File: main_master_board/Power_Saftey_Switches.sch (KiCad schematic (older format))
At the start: 2 parts

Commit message: Added lots of things. current/voltage monitoring. and other stuff
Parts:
- added C?: 48nF, symbol C_Small
- added C?: 2uF, symbol C_Small
- added C? (x2): 100nF, symbol C_Small
- added C?: 100uF, symbol C_Small
- added C?: 100nF, symbol C
- added D? (x2): DA2S10100L, symbol D_Small
- added P?: CONN_01X05, symbol CONN_01X05
- added Q?: LT1910, SO_8, symbol LT1910
- added R?: 0.0025, symbol R
- added R? (x3): 5K, symbol R
- added R? (x2): 1K, symbol R
- added R? (x3): 10K, symbol R
- added SW?: SWITCH_SPST, symbol SWITCH_SPST
- added U?: 74HC1G126, symbol 74AHC1G126
- added U?: PIC12(L)F1571/2, symbol PIC12(L)F1571/2
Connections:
- net labels added: 3V3, GND, KS_nFault, KS_physical_in, KS_physical_out, KS_uC, KS_watchdog, MCLR_KS, Motor_en, PGEC_KS, PGED_KS, Sense, Vmain, Vmotors, main_gate, uC_KS_1, uC_KS_2
- wire segments 7 -> 106
- no-connect marks 0 -> 1
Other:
- note added: "Do not get\n74HCT1G126\nvariant"
- note added: "KS_uC"
- note added: "KS_uC_programmer"
- note added: "Manual switch to \nturn motors off"
- note added: "TVS to \nkeep <20V"
- moved on the sheet: D?, Q?

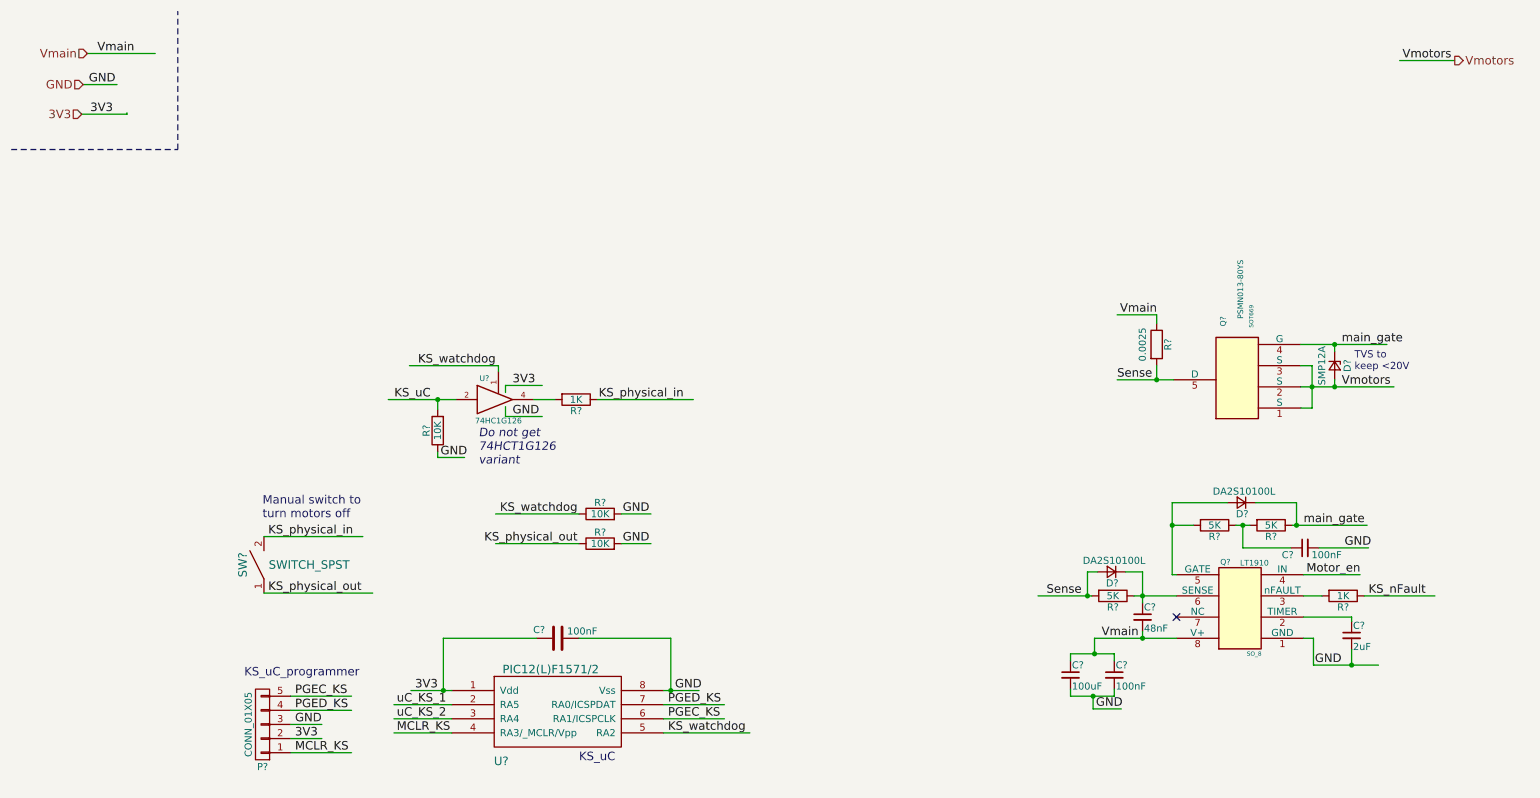
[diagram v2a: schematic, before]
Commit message: Updated some of the schematics and started assigning footprints
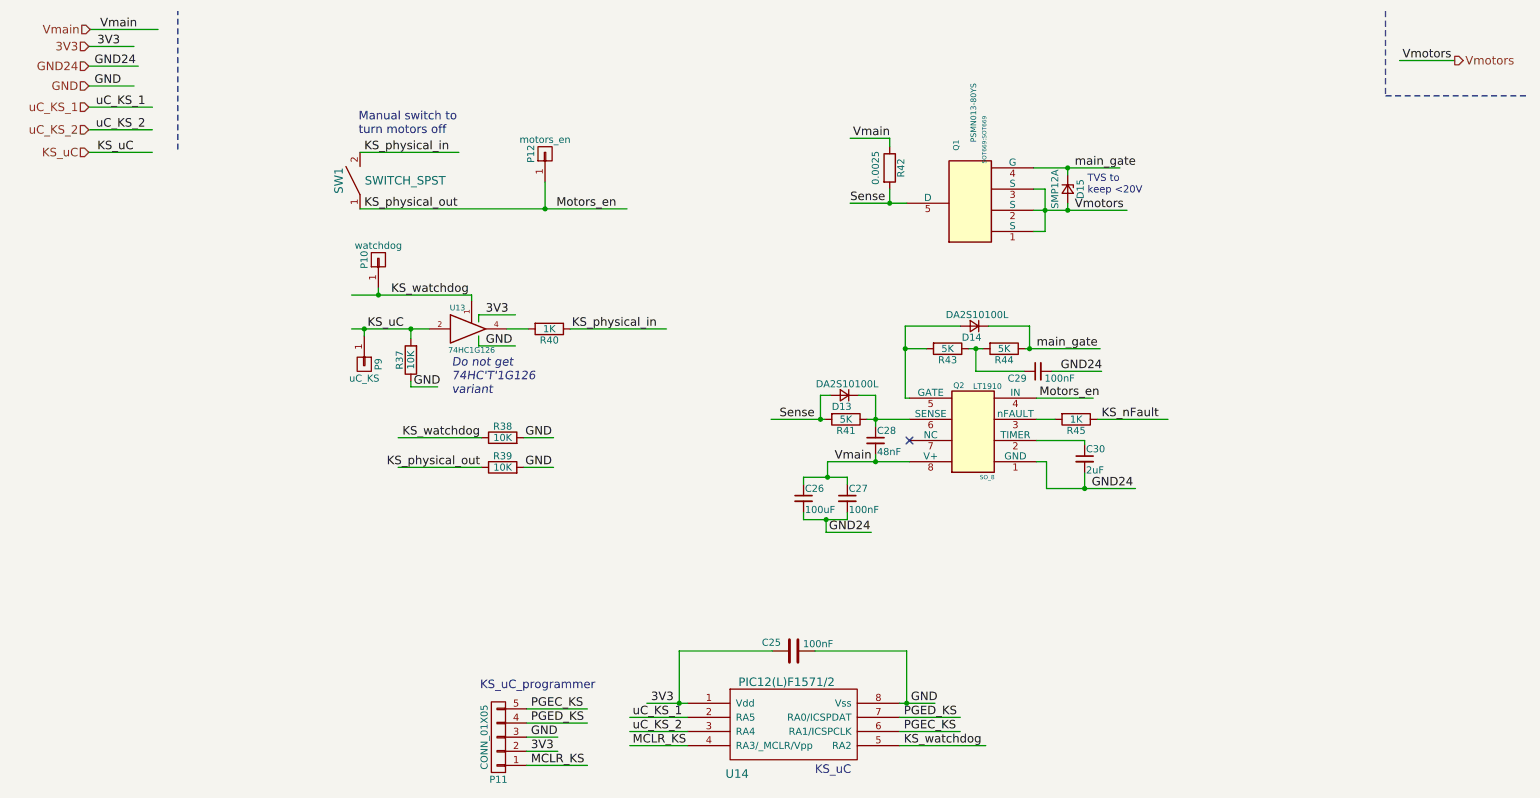
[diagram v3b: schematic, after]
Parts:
- added P10: watchdog, symbol CONN_01X01
- added P12: motors_en, symbol CONN_01X01
- added P9: uC_KS, symbol CONN_01X01
- Q1: renamed from Q?; footprint SOT669 -> SOT669:SOT669
- gave numbers to parts that had none: 23
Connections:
- net labels added: GND24, Motors_en
- net labels removed: Motor_en
- wire segments 106 -> 94
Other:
- note added: "Do not get\n74HC'T'1G126\nvariant"
- note removed: "Do not get\n74HCT1G126\nvariant"
- moved on the sheet: C25, C26, C27, C28, C29, C30, D13, D14, D15, P11, Q1, Q2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

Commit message: Updating the footprints and components list. still working on it
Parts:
- R37, R38, R39, R40, R41, R42, R43, R44, R45: footprint (none) -> Resistors_SMD:R_0603
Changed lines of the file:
@@
 LIBS:FDS4935A
 LIBS:Si1900DL
-LIBS:Amplifiers
-LIBS:Connectors
-LIBS:DataStorage
-LIBS:Diodes
-LIBS:Microprocessors
-LIBS:MiscellaneousDevices
-LIBS:Passives
-LIBS:PMOD
-LIBS:PowerComponents
-LIBS:RepeaterParts
-LIBS:RF_OEM_Parts
 LIBS:Sensors
-LIBS:TransistorParts
 LIBS:LP3852-3.3
 LIBS:0s102011ma1qn1
@@
 F 0 "R42" V 6780 1590 50  0000 C CNN
 F 1 "0.0025" V 6600 1590 50  0000 C CNN
-F 2 "" V 6630 1590 50  0001 C CNN
+F 2 "Resistors_SMD:R_0603" V 6630 1590 50  0001 C CNN
 F 3 "" H 6700 1590 50  0000 C CNN
 	1    6700 1590
@@
 F 0 "R41" V 6470 3370 50  0000 C CNN
 F 1 "5K" V 6390 3370 50  0000 C CNN
-F 2 "" V 6320 3370 50  0001 C CNN
+F 2 "Resistors_SMD:R_0603" V 6320 3370 50  0001 C CNN
 F 3 "" H 6390 3370 50  0000 C CNN
 	1    6390 3370
@@
 F 0 "R45" V 8100 3370 50  0000 C CNN
 F 1 "1K" V 8020 3370 50  0000 C CNN
-F 2 "" V 7950 3370 50  0001 C CNN
+F 2 "Resistors_SMD:R_0603" V 7950 3370 50  0001 C CNN
 F 3 "" H 8020 3370 50  0000 C CNN
 	1    8020 3370
@@
 F 0 "R43" V 7190 2870 50  0000 C CNN
 F 1 "5K" V 7110 2870 50  0000 C CNN
-F 2 "" V 7040 2870 50  0001 C CNN
+F 2 "Resistors_SMD:R_0603" V 7040 2870 50  0001 C CNN
 F 3 "" H 7110 2870 50  0000 C CNN
 	1    7110 2870
@@
 F 0 "R44" V 7590 2870 50  0000 C CNN
 F 1 "5K" V 7510 2870 50  0000 C CNN
-F 2 "" V 7440 2870 50  0001 C CNN
+F 2 "Resistors_SMD:R_0603" V 7440 2870 50  0001 C CNN
 F 3 "" H 7510 2870 50  0000 C CNN
 	1    7510 2870
@@
 F 0 "R40" V 4370 2730 50  0000 C CNN
 F 1 "1K" V 4290 2730 50  0000 C CNN
-F 2 "" V 4220 2730 50  0001 C CNN
+F 2 "Resistors_SMD:R_0603" V 4220 2730 50  0001 C CNN
 F 3 "" H 4290 2730 50  0000 C CNN
 	1    4290 2730
@@
 F 0 "R37" V 3390 2950 50  0000 C CNN
 F 1 "10K" V 3310 2950 50  0000 C CNN
-F 2 "" V 3240 2950 50  0001 C CNN
+F 2 "Resistors_SMD:R_0603" V 3240 2950 50  0001 C CNN
 F 3 "" H 3310 2950 50  0000 C CNN
 	1    3310 2950
@@
 F 0 "R38" V 4040 3500 50  0000 C CNN
 F 1 "10K" V 3960 3500 50  0000 C CNN
-F 2 "" V 3890 3500 50  0001 C CNN
+F 2 "Resistors_SMD:R_0603" V 3890 3500 50  0001 C CNN
 F 3 "" H 3960 3500 50  0000 C CNN
 	1    3960 3500
@@
 F 0 "R39" V 4040 3710 50  0000 C CNN
 F 1 "10K" V 3960 3710 50  0000 C CNN
-F 2 "" V 3890 3710 50  0001 C CNN
+F 2 "Resistors_SMD:R_0603" V 3890 3710 50  0001 C CNN
 F 3 "" H 3960 3710 50  0000 C CNN
 	1    3960 3710

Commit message: I did a lot of things
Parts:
- C25, C27, C28, C29, C30: footprint (none) -> Capacitors_SMD:C_0603
- C26: footprint (none) -> Capacitors_SMD:C_1206
- D13, D14: footprint (none) -> SSMini2-F5-B:SSMini2-F5-B
- D15: footprint (none) -> DO-220AA:DO-220AA
- P10, P12, P9: footprint (none) -> Socket_Strips:Socket_Strip_Straight_1x01
- P11: footprint (none) -> Socket_Strips:Socket_Strip_Straight_1x05
- Q2: footprint SO_8 -> dp_devices:dp_devices-SO-8
- SW1: footprint (none) -> molex_microclasp:55935-0210
- U13: footprint (none) -> TO_SOT_Packages_SMD:SOT-353
- U14: footprint (none) -> dp_devices:dp_devices-SOIC-8
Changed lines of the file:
@@
 LIBS:FDS4935A
 LIBS:Si1900DL
+LIBS:Amplifiers
+LIBS:Connectors
+LIBS:DataStorage
+LIBS:Diodes
+LIBS:Microprocessors
+LIBS:MiscellaneousDevices
+LIBS:Passives
+LIBS:PMOD
+LIBS:PowerComponents
+LIBS:RepeaterParts
+LIBS:RF_OEM_Parts
 LIBS:Sensors
+LIBS:TransistorParts
 LIBS:LP3852-3.3
 LIBS:0s102011ma1qn1
@@
 LIBS:xal5050-562meb
 LIBS:xal6030-182mec
+LIBS:decaWave
 LIBS:main_master_board-cache
 EELAYER 25 0
@@
 $Descr A4 11693 8268
 encoding utf-8
-Sheet 3 4
+Sheet 5 5
 Title ""
 Date ""
@@
 F 0 "D15" H 7960 1830 50  0000 C CNN
 F 1 "SMP12A" H 7960 1650 50  0000 C CNN
-F 2 "" V 7960 1740 50  0001 C CNN
+F 2 "DO-220AA:DO-220AA" V 7960 1740 50  0001 C CNN
 F 3 "" V 7960 1740 50  0000 C CNN
 	1    7960 1740
@@
 F 0 "Q2" V 7630 3610 40  0000 R CNN
 F 1 "LT1910" V 7600 3470 40  0000 R TNN
-F 2 "SO_8" V 6980 3370 30  0000 C CNN
+F 2 "dp_devices:dp_devices-SO-8" V 6980 3370 30  0000 C CNN
 F 3 "" H 7290 3470 60  0000 C CNN
 	1    7290 3470
@@
 F 0 "D13" H 6330 3280 50  0000 L CNN
 F 1 "DA2S10100L" H 6140 3120 50  0000 L CNN
-F 2 "" H 6380 3200 50  0001 C CNN
+F 2 "SSMini2-F5-B:SSMini2-F5-B" H 6380 3200 50  0001 C CNN
 F 3 "http://datasheet.octopart.com/DA2S10100L-Panasonic-datasheet-13317586.pdf" H 6380 3200 50  0001 C CNN
 	1    6380 3200
@@
 F 0 "C28" H 6610 3590 50  0000 L CNN
 F 1 "48nF" H 6610 3440 50  0000 L CNN
-F 2 "" H 6600 3520 50  0001 C CNN
+F 2 "Capacitors_SMD:C_0603" H 6600 3520 50  0001 C CNN
 F 3 "" H 6600 3520 50  0000 C CNN
 	1    6600 3520
@@
 F 0 "C30" H 8090 3720 50  0000 L CNN
 F 1 "2uF" H 8090 3570 50  0000 L CNN
-F 2 "" H 8080 3650 50  0001 C CNN
+F 2 "Capacitors_SMD:C_0603" H 8080 3650 50  0001 C CNN
 F 3 "" H 8080 3650 50  0000 C CNN
 	1    8080 3650
@@
 F 0 "C29" V 7700 3110 50  0000 L CNN
 F 1 "100nF" V 7700 2770 50  0000 L CNN
-F 2 "" H 7750 3030 50  0001 C CNN
+F 2 "Capacitors_SMD:C_0603" H 7750 3030 50  0001 C CNN
 F 3 "" H 7750 3030 50  0000 C CNN
 	1    7750 3030
@@
 F 0 "D14" H 7250 2790 50  0000 L CNN
 F 1 "DA2S10100L" H 7060 2630 50  0000 L CNN
-F 2 "" H 7300 2710 50  0001 C CNN
+F 2 "SSMini2-F5-B:SSMini2-F5-B" H 7300 2710 50  0001 C CNN
 F 3 "http://datasheet.octopart.com/DA2S10100L-Panasonic-datasheet-13317586.pdf" H 7300 2710 50  0001 C CNN
 	1    7300 2710
@@
 F 0 "C26" H 6100 4000 50  0000 L CNN
 F 1 "100uF" H 6100 3850 50  0000 L CNN
-F 2 "" H 6090 3930 50  0001 C CNN
+F 2 "Capacitors_SMD:C_1206" H 6090 3930 50  0001 C CNN
 F 3 "" H 6090 3930 50  0000 C CNN
 	1    6090 3930
@@
 F 0 "C27" H 6410 4000 50  0000 L CNN
 F 1 "100nF" H 6410 3850 50  0000 L CNN
-F 2 "" H 6400 3930 50  0001 C CNN
+F 2 "Capacitors_SMD:C_0603" H 6400 3930 50  0001 C CNN
 F 3 "" H 6400 3930 50  0000 C CNN
 	1    6400 3930
@@
 F 0 "U13" H 3640 2880 40  0000 C CNN
 F 1 "74HC1G126" H 3740 2580 40  0000 C CNN
-F 2 "" H 3740 2730 60  0001 C CNN
+F 2 "TO_SOT_Packages_SMD:SOT-353" H 3740 2730 60  0001 C CNN
 F 3 "" H 3740 2730 60  0000 C CNN
 	1    3740 2730
@@
 F 0 "U14" H 5620 5680 60  0000 C CNN
 F 1 "PIC12(L)F1571/2" H 5970 6330 60  0000 C CNN
-F 2 "" H 5570 5780 60  0001 C CNN
+F 2 "dp_devices:dp_devices-SOIC-8" H 5570 5780 60  0001 C CNN
 F 3 "" H 5570 5780 60  0000 C CNN
 	1    5570 5780
@@
 F 0 "C25" V 6080 5100 50  0000 L CNN
 F 1 "100nF" V 6070 4730 50  0000 L CNN
-F 2 "" H 6058 4860 50  0001 C CNN
+F 2 "Capacitors_SMD:C_0603" H 6058 4860 50  0001 C CNN
 F 3 "" H 6020 5010 50  0000 C CNN
 	1    6020 5010
@@
 F 0 "P11" H 3930 5920 50  0000 C CNN
 F 1 "CONN_01X05" V 4030 5620 50  0000 C CNN
-F 2 "" H 3930 5620 50  0001 C CNN
+F 2 "Socket_Strips:Socket_Strip_Straight_1x05" H 3930 5620 50  0001 C CNN
 F 3 "" H 3930 5620 50  0000 C CNN
 	1    3930 5620
@@
 F 0 "SW1" H 2950 1830 60  0000 C CNN
 F 1 "SWITCH_SPST" V 2950 1360 60  0000 C CNN
-F 2 "" H 2950 1680 60  0001 C CNN
+F 2 "molex_microclasp:55935-0210" H 2950 1680 60  0001 C CNN
 F 3 "" H 2950 1680 60  0000 C CNN
 	1    2950 1680
@@
 F 0 "P12" H 4260 1590 50  0000 C CNN
 F 1 "motors_en" V 4360 1490 50  0000 C CNN
-F 2 "" H 4260 1490 50  0001 C CNN
+F 2 "Socket_Strips:Socket_Strip_Straight_1x01" H 4260 1490 50  0001 C CNN
 F 3 "" H 4260 1490 50  0000 C CNN
 	1    4260 1490
@@
 F 0 "P10" H 3080 2340 50  0000 C CNN
 F 1 "watchdog" V 3180 2240 50  0000 C CNN
-F 2 "" H 3080 2240 50  0001 C CNN
+F 2 "Socket_Strips:Socket_Strip_Straight_1x01" H 3080 2240 50  0001 C CNN
 F 3 "" H 3080 2240 50  0000 C CNN
 	1    3080 2240
@@
 F 0 "P9" H 2980 3080 50  0000 C CNN
 F 1 "uC_KS" V 3080 2980 50  0000 C CNN
-F 2 "" H 2980 2980 50  0001 C CNN
+F 2 "Socket_Strips:Socket_Strip_Straight_1x01" H 2980 2980 50  0001 C CNN
 F 3 "" H 2980 2980 50  0000 C CNN
 	1    2980 2980

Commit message: Didn't save before pushing last commit
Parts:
- SW1: footprint molex_microclasp:55935-0210 -> molex_microclasp2:microclasp_vdrx2
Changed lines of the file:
@@
 LIBS:xal6030-182mec
 LIBS:decaWave
+LIBS:TPS61232DRC
 LIBS:main_master_board-cache
 EELAYER 25 0
@@
 F 0 "SW1" H 2950 1830 60  0000 C CNN
 F 1 "SWITCH_SPST" V 2950 1360 60  0000 C CNN
-F 2 "molex_microclasp:55935-0210" H 2950 1680 60  0001 C CNN
+F 2 "molex_microclasp2:microclasp_vdrx2" H 2950 1680 60  0001 C CNN
 F 3 "" H 2950 1680 60  0000 C CNN
 	1    2950 1680

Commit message: Moved library files to dedicated folder. Added support for Edison and Open-Q 410 boards.
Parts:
- P10, P12, P9: footprint Socket_Strips:Socket_Strip_Straight_1x01 -> SMD_Packages:1Pin
- P11: footprint Socket_Strips:Socket_Strip_Straight_1x05 -> SMD_pinheader:01x05_pinheader_SMD; Field4 (none) -> http://www.digikey.com/product-detail/en/3m/961105-6300-AR-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
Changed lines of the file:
@@
 LIBS:USB_CONSOL-SchDoc-cache
 LIBS:VBAT_PROTECTION_REGS-SchDoc-cache
-LIBS:LMR16020
-LIBS:TPS832130SIL
 LIBS:TPS754
-LIBS:TPS61089
 LIBS:FDS4935A
 LIBS:Si1900DL
@@
 LIBS:xal6030-182mec
 LIBS:decaWave
+LIBS:conn_2x50
+LIBS:conn_open_q_x2
+LIBS:LMR16020
+LIBS:TPS61089
 LIBS:TPS61232DRC
+LIBS:TPS832130SIL
+LIBS:SS4-50-3.00-X-D
 LIBS:main_master_board-cache
 EELAYER 25 0
@@
 $Descr A4 11693 8268
 encoding utf-8
-Sheet 3 5
+Sheet 3 6
 Title ""
 Date ""
@@
 F 0 "P11" H 3930 5920 50  0000 C CNN
 F 1 "CONN_01X05" V 4030 5620 50  0000 C CNN
-F 2 "Socket_Strips:Socket_Strip_Straight_1x05" H 3930 5620 50  0001 C CNN
+F 2 "SMD_pinheader:01x05_pinheader_SMD" H 3930 5620 50  0001 C CNN
 F 3 "" H 3930 5620 50  0000 C CNN
+F 4 "http://www.digikey.com/product-detail/en/3m/961105-6300-AR-PR/3M9487CT-ND/2071622" H 3930 5620 60  0001 C CNN "Field4"
 	1    3930 5620
 	-1   0    0    1
@@
 F 0 "P12" H 4260 1590 50  0000 C CNN
 F 1 "motors_en" V 4360 1490 50  0000 C CNN
-F 2 "Socket_Strips:Socket_Strip_Straight_1x01" H 4260 1490 50  0001 C CNN
+F 2 "SMD_Packages:1Pin" H 4260 1490 50  0001 C CNN
 F 3 "" H 4260 1490 50  0000 C CNN
 	1    4260 1490
@@
 F 0 "P10" H 3080 2340 50  0000 C CNN
 F 1 "watchdog" V 3180 2240 50  0000 C CNN
-F 2 "Socket_Strips:Socket_Strip_Straight_1x01" H 3080 2240 50  0001 C CNN
+F 2 "SMD_Packages:1Pin" H 3080 2240 50  0001 C CNN
 F 3 "" H 3080 2240 50  0000 C CNN
 	1    3080 2240
@@
 F 0 "P9" H 2980 3080 50  0000 C CNN
 F 1 "uC_KS" V 3080 2980 50  0000 C CNN
-F 2 "Socket_Strips:Socket_Strip_Straight_1x01" H 2980 2980 50  0001 C CNN
+F 2 "SMD_Packages:1Pin" H 2980 2980 50  0001 C CNN
 F 3 "" H 2980 2980 50  0000 C CNN
 	1    2980 2980
